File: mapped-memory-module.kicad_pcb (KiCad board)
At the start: 2 copper layers, 99.8 x 99.8 mm, 20 parts, among them J1 Conn_01x02_Male, J2 Conn_01x02_Male, J3 Conn_02x30_Odd_Even, U1 74HC00, U10 74HC02, U12 74HC21, U14 74HC21, U15 74HC375, U16 74HC375, U2 74HC04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

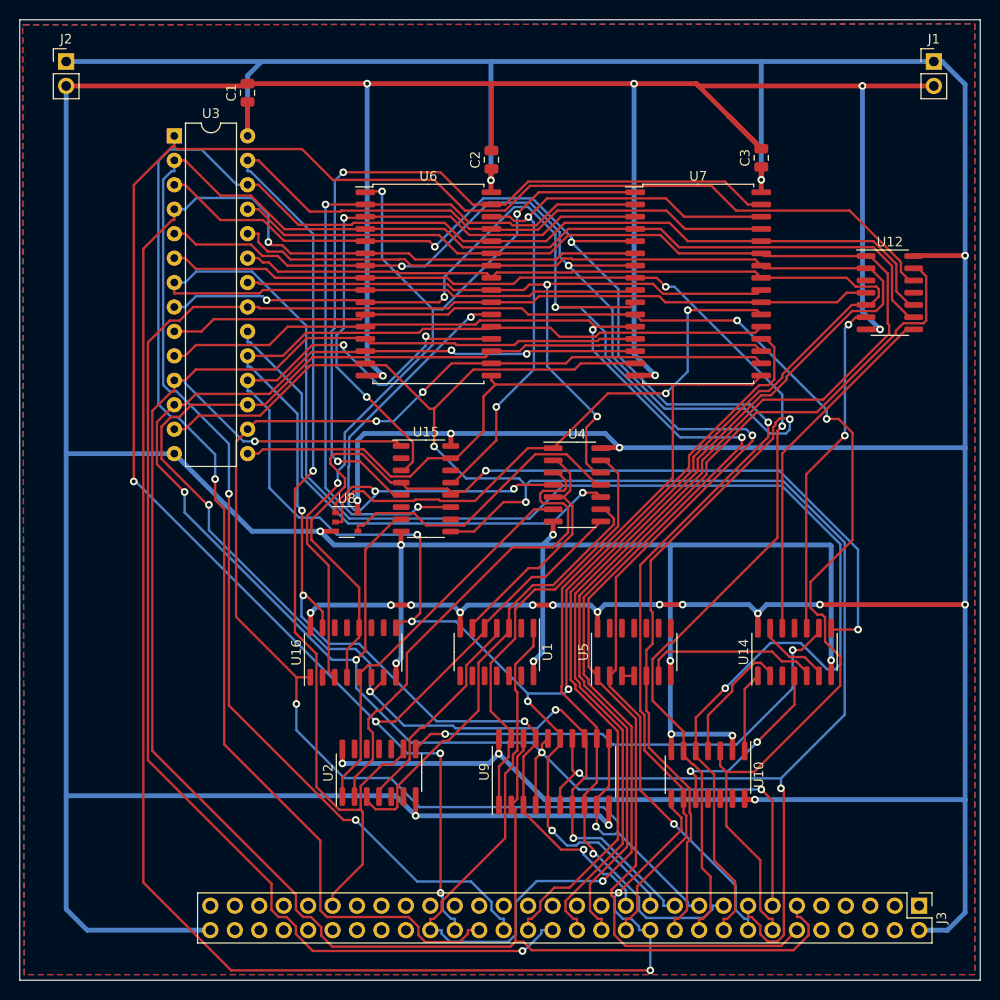
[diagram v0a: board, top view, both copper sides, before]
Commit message: add mapped memory lane
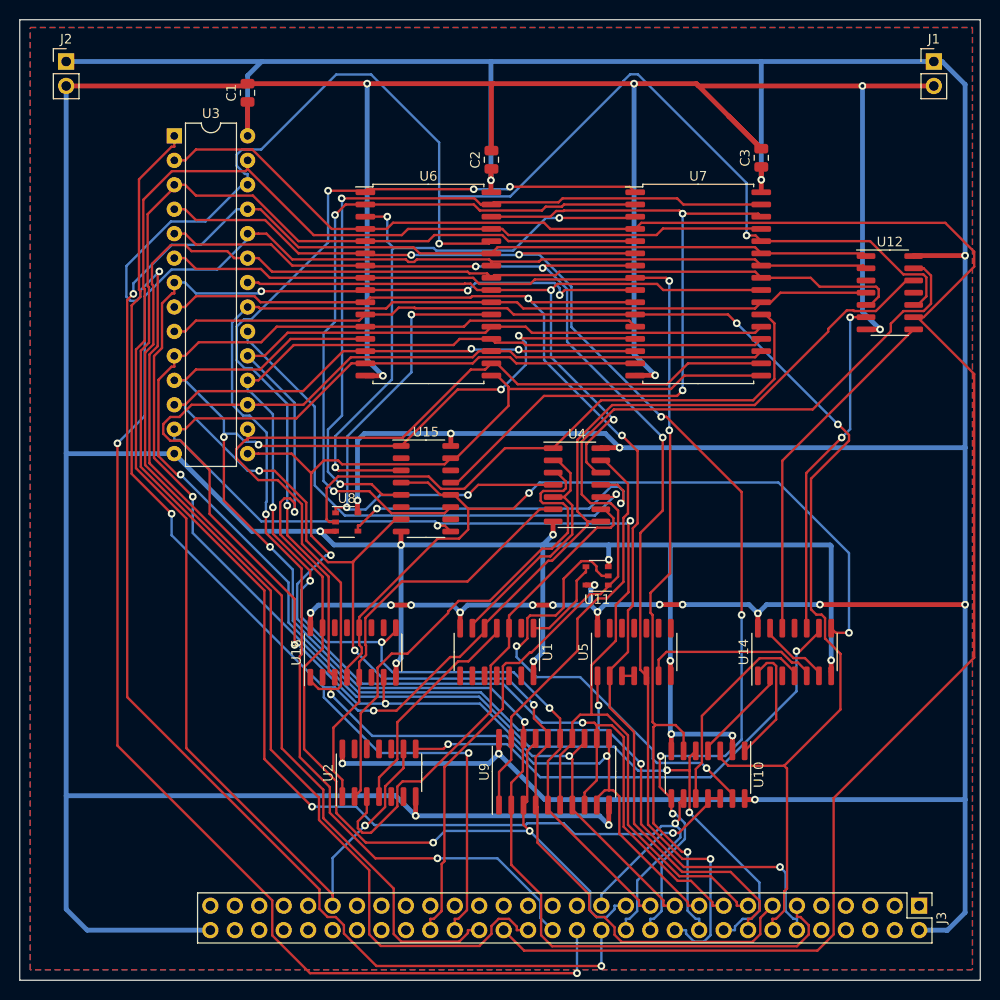
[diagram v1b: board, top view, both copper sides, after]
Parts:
- added U11: 74AHC1G08, Package_SO:TSOP-5_1.65x3.05mm_P0.95mm, F.Cu at (84.9, 84.5)
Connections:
- J3 pad 27: unconnected-(J3-Pad27) -> MAPPED_MEM
- U1 pad 1: A15 -> Net-(U1-Pad1)
- U10 pad 11: unconnected-(U10-Pad11) -> MAPPED_MEM
- U10 pad 12: unconnected-(U10-Pad12) -> MAPPED_MEM
- U10 pad 13: unconnected-(U10-Pad13) -> Net-(U10-Pad13)
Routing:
- net A6: track 204.8 -> 141.7 mm, vias 3 -> 6
- net Net-(U10-Pad13): track 0.00 -> 47.6 mm, vias 0 -> 2
- net A13: track 193.5 -> 233.3 mm, vias 1 -> 3
- net A15: track 146.9 -> 111.3 mm, vias 1 -> 0
- net A9: track 157.2 -> 192.3 mm, vias 0 -> 2
- net A3: track 199.6 -> 165.3 mm, vias 1 -> 6
- net D0: track 221.3 -> 188.4 mm, vias 1 -> 6
- net A8: track 160.5 -> 191.4 mm, vias 0 -> 2
- net A7: track 150.2 -> 180.9 mm, vias 3 -> 2
- net D2: track 196.3 -> 168.8 mm, vias 4 -> 2
- net D6: track 169.9 -> 143.3 mm, vias 7 -> 4
- net A11: track 156.1 -> 180.3 mm
- net A14: track 218.4 -> 195.0 mm, vias 4 -> 3
- net A2: track 154.1 -> 130.9 mm, vias 5 -> 2
- net A10: track 174.3 -> 152.8 mm, vias 1 -> 2
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- added copper zone on B.Cu, net GND
- added copper zone on F.Cu, net GND
- removed copper zone on B.Cu, net (none)
- removed copper zone on F.Cu, net (none)
